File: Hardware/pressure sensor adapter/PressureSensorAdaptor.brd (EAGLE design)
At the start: 29.2 x 30.5 mm, 11 parts, among them IC1 RCV420P

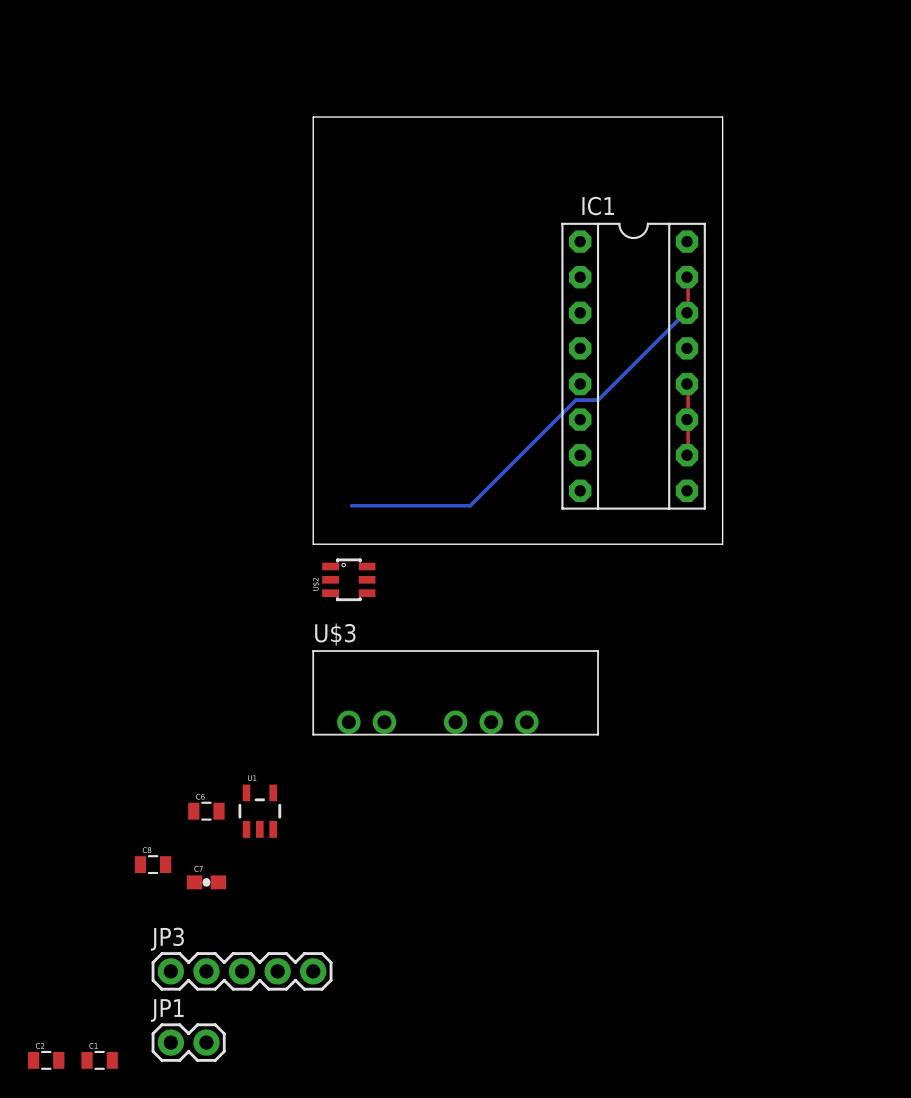
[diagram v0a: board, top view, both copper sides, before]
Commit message: routed alternet Pressure sense adapter board
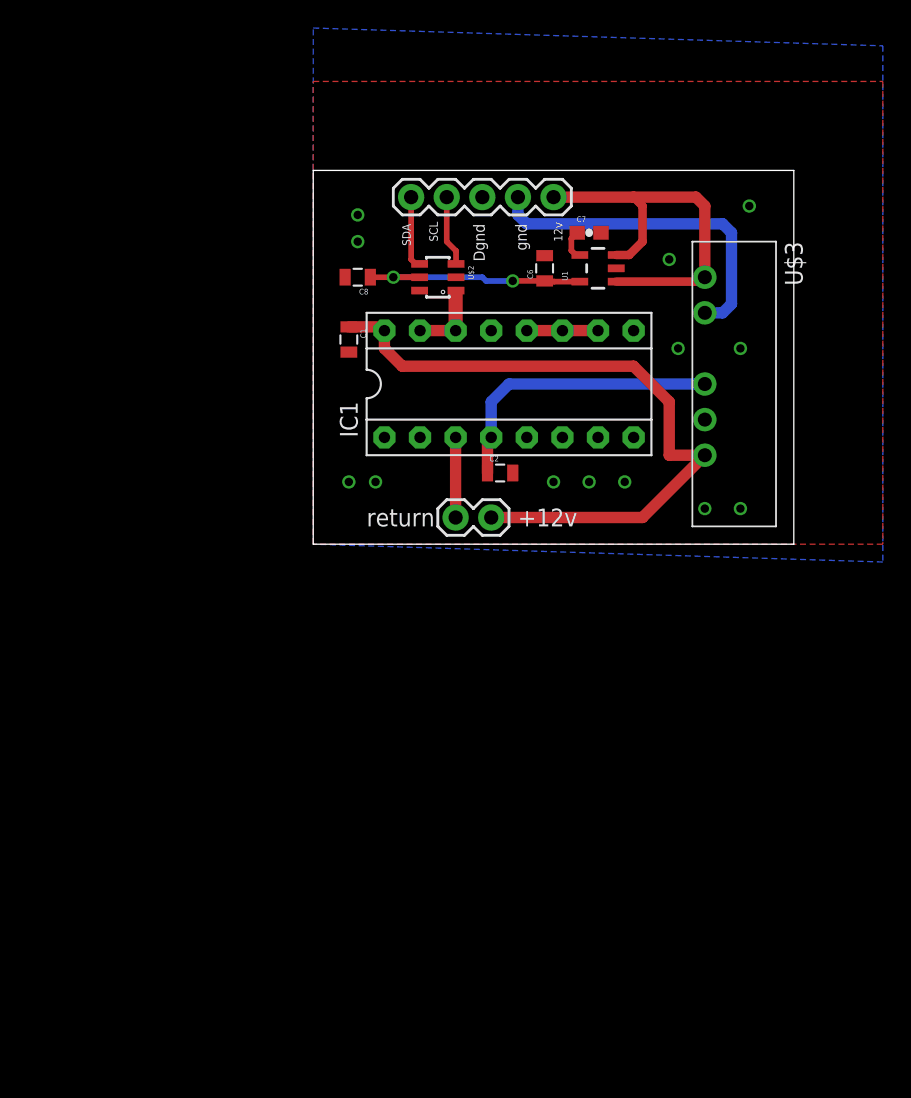
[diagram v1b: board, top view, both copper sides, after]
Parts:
- moved JP3 57.8 mm to (6.99, 24.8)
- moved C1 54.4 mm to (2.54, 14.6), turned to 270 degrees
- moved C7 53.8 mm to (19.7, 22.2)
- moved C2 53.0 mm to (13.3, 5.08)
- moved C6 45.6 mm to (16.5, 19.7), turned to 90 degrees
- moved U1 45.6 mm to (20.3, 19.7), turned to 90 degrees
- moved C8 44.4 mm to (3.17, 19.1), turned to 180 degrees
- moved JP1 42.6 mm to (10.2, 1.91)
- moved U$3 40.7 mm to (27.9, 19.1), turned to 270 degrees
- moved U$2 22.5 mm to (8.89, 19.1), turned to 180 degrees
- moved IC1 8.98 mm to (14.0, 11.4), turned to 0 degrees
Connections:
- removed net VIN: JP3.5, U$3.P$1, U1.1, U1.3
- new net 12V+: C1.1, IC1.16, JP1.2, U$3.P$6
- new net 12V-: C2.1, IC1.4, U$3.P$4
- net 12V: now also JP3.5, U$3.P$1, U1.1, U1.3; no longer C1.1, C2.1, IC1.16, IC1.4, JP1.2, U$3.P$4, U$3.P$6
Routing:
- net 12V+: track 0.00 -> 49.2 mm
- net 12V: track 0.00 -> 28.3 mm
- net GND: track 0.00 -> 24.3 mm
- net VOUT: track 32.2 -> 7.95 mm
- net 12V-: track 0.00 -> 21.0 mm
- net 5V: track 0.00 -> 16.9 mm, vias 0 -> 2
- net N$2: track 0.00 -> 5.71 mm
- net SDA: track 0.00 -> 5.18 mm
- net SCL: track 0.00 -> 5.04 mm
- net N$11: track 0.00 -> 2.18 mm
- added copper zone on layer 1, net GND-ISO
- added copper zone on layer 16, net GND-ISO
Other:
- board size 29.2 x 30.5 mm -> 34.3 x 26.7 mm
- board text added: "+12v"
- board text added: "12v"
- board text added: "Dgnd"
- board text added: "SCL"
- board text added: "SDA"
- board text added: "gnd"
- board text added: "return"

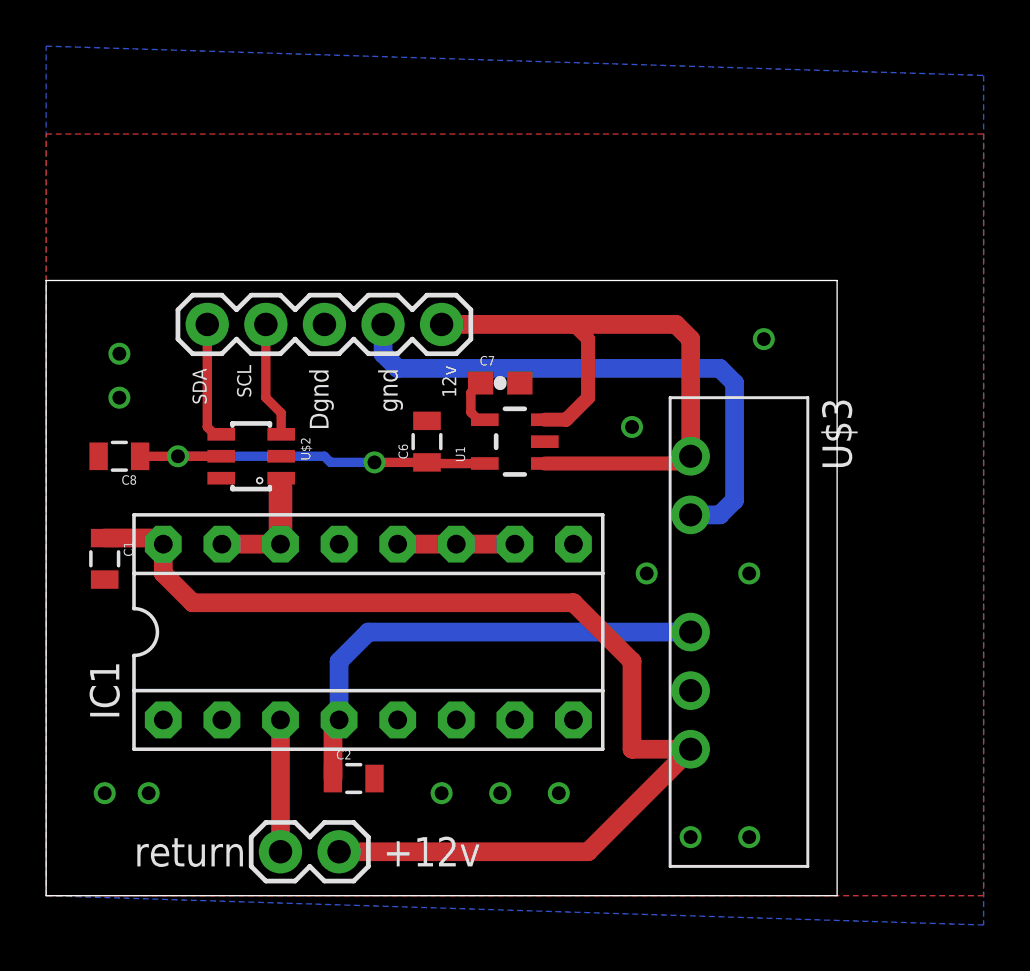
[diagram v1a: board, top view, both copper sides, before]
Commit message: added frame and logo to loayout
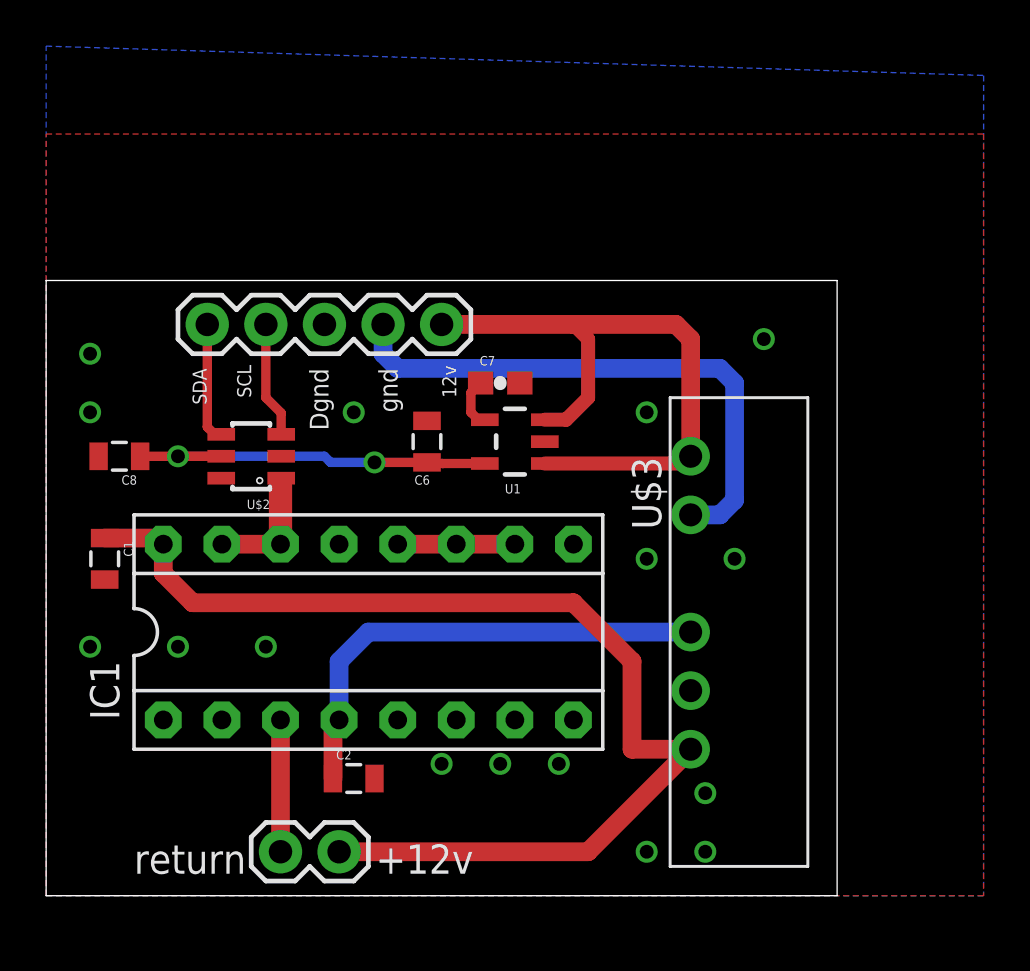
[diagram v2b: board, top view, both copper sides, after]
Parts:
- added FRAME1: FRAME-LEDGER, SparkFun-Aesthetics:CREATIVE_COMMONS
- added U$1: (no value), RitLaunchInitiative:RITLAUNCH_LOGO_SMALLB
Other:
- board text added: "Pressure sensor Adapter"
- board text added: "RIT Launch Initative"
- board text added: "Rev:A"
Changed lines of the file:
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@@
 <setting verticaltext="up"/>
 </settings>
-<grid distance="1.27" unitdist="mm" unit="mm" style="lines" multiple="1" display="yes" altdistance="0.025" altunitdist="inch" altunit="inch"/>
+<grid distance="1.27" unitdist="mm" unit="inch" style="lines" multiple="1" display="yes" altdistance="0.0125" altunitdist="inch" altunit="inch"/>
 <layers>
 <layer number="1" name="Top" color="4" fill="1" visible="yes" active="yes"/>
@@
 <wire x1="34.29" y1="26.67" x2="0" y2="26.67" width="0" layer="20"/>
 <wire x1="0" y1="26.67" x2="0" y2="0" width="0" layer="20"/>
-<text x="14.605" y="1.27" size="1.27" layer="21">+12v</text>
-<text x="3.81" y="1.27" size="1.27" layer="21">return</text>
+<text x="14.2875" y="0.9525" size="1.27" layer="21">+12v</text>
+<text x="3.81" y="0.9525" size="1.27" layer="21">return</text>
 <text x="6.35" y="22.86" size="0.6096" layer="21" rot="R270">SDA</text>
 <text x="8.89" y="21.59" size="0.6096" layer="21" rot="R90">SCL</text>
@@
 <text x="11.43" y="22.86" size="0.8128" layer="21" rot="R270">Dgnd</text>
 <text x="15.24" y="20.955" size="0.8128" layer="21" rot="R90">gnd</text>
+<text x="31.75" y="1.5875" size="1.27" layer="22" rot="MR90">Pressure sensor Adapter</text>
+<text x="30.1625" y="18.0975" size="0.8128" layer="22" rot="MR90">Rev:A</text>
+<text x="31.115" y="11.7475" size="0.8128" layer="22" rot="MR270">RIT Launch Initative</text>
 </plain>
 <attributes>
@@
 </class>
 </classes>
-<designrules name="LaenPCBOrder">
+<designrules name="LaenPCBOrder *">
 <description language="de">&lt;b&gt;EAGLE Design Rules&lt;/b&gt;
 &lt;p&gt;
@@
 <param name="mlMinCreamFrame" value="0mil"/>
 <param name="mlMaxCreamFrame" value="0mil"/>
-<param name="mlViaStopLimit" value="0mil"/>
+<param name="mlViaStopLimit" value="15mil"/>
 <param name="srRoundness" value="0"/>
 <param name="srMinRoundness" value="0mil"/>
@@
 </autorouter>
 <elements>
-<element name="IC1" library="burr-brown" package="DIL16" value="RCV420P" x="13.97" y="11.43">
+<element name="IC1" library="burr-brown" package="DIL16" value="RCV420P" x="13.97" y="11.43" smashed="yes">
 <attribute name="OC_NEWARK" value="60K6765" x="13.97" y="11.43" size="1.778" layer="27" display="off"/>
 <attribute name="MPN" value="RCV420JP" x="13.97" y="11.43" size="1.778" layer="27" display="off"/>
 <attribute name="MF" value="TEXAS INSTRUMENTS" x="13.97" y="11.43" size="1.778" layer="27" display="off"/>
 <attribute name="OC_FARNELL" value="1212342" x="13.97" y="11.43" size="1.778" layer="27" display="off"/>
-</element>
-<element name="U$2" library="RitLaunchInitiative" package="SOT23-6" value="MCP3425" x="8.89" y="19.05" rot="R180"/>
+<attribute name="VALUE" x="14.9225" y="9.2075" size="1.27" layer="27" ratio="10"/>
+<attribute name="NAME" x="3.175" y="7.62" size="1.27" layer="25" ratio="10" rot="R90"/>
+</element>
+<element name="U$2" library="RitLaunchInitiative" package="SOT23-6" value="MCP3425" x="8.89" y="19.05" smashed="yes" rot="R180">
+<attribute name="NAME" x="8.6995" y="16.764" size="0.4064" layer="25"/>
+</element>
 <element name="U$3" library="RitLaunchInitiative" package="VASD1-S12-D12-SIP" value="VASD1-S12-D12-SIP" x="27.94" y="19.05" smashed="yes" rot="R270">
-<attribute name="NAME" x="33.655" y="21.59" size="1.27" layer="25" rot="R270"/>
-<attribute name="VALUE" x="31.115" y="18.415" size="1.27" layer="27" rot="R270"/>
-</element>
-<element name="U1" library="SparkFun-PowerIC" package="SOT23-5" value="" x="20.32" y="19.685" rot="R90">
+<attribute name="NAME" x="26.67" y="15.875" size="1.27" layer="25" rot="R90"/>
+</element>
+<element name="U1" library="SparkFun-PowerIC" package="SOT23-5" value="" x="20.32" y="19.685" smashed="yes" rot="R90">
 <attribute name="PROD_ID" value="VREG-00823" x="20.32" y="19.685" size="1.778" layer="27" rot="R90" display="off"/>
-</element>
-<element name="C6" library="SparkFun-Capacitors" package="0805" value="2.2uF" x="16.51" y="19.685" rot="R90">
+<attribute name="NAME" x="20.574" y="17.8435" size="0.4064" layer="25" rot="R180"/>
+<attribute name="VALUE" x="20.5105" y="18.7325" size="0.4064" layer="27" rot="R90"/>
+</element>
+<element name="C6" library="SparkFun-Capacitors" package="0805" value="2.2uF" x="16.51" y="19.685" smashed="yes" rot="R90">
 <attribute name="PROD_ID" value="CAP-11624" x="16.51" y="19.685" size="1.778" layer="27" rot="R90" display="off"/>
-</element>
-<element name="C7" library="SparkFun-Capacitors" package="0603-CAP" value="470pF" x="19.685" y="22.225">
+<attribute name="NAME" x="16.637" y="18.2245" size="0.4064" layer="25" rot="R180"/>
+</element>
+<element name="C7" library="SparkFun-Capacitors" package="0603-CAP" value="470pF" x="19.685" y="22.225" smashed="yes">
 <attribute name="PROD_ID" value="CAP-07884" x="19.685" y="22.225" size="1.778" layer="27" display="off"/>
+<attribute name="NAME" x="18.796" y="22.987" size="0.4064" layer="25" font="vector"/>
 </element>
 <element name="C8" library="SparkFun-Capacitors" package="0805" value="" x="3.175" y="19.05" rot="R180"/>
@@
 <attribute name="PROD_ID" value="CAP-11625" x="13.335" y="5.08" size="1.778" layer="27" display="off"/>
 </element>
+<element name="FRAME1" library="SparkFun-Aesthetics" package="CREATIVE_COMMONS" value="FRAME-LEDGER" x="-5.08" y="-3.81">
+<attribute name="VERSION" value="A" x="-5.08" y="-3.81" size="1.778" layer="27" display="off"/>
+<attribute name="DESIGNER" value="Roy Cohen" x="-5.08" y="-3.81" size="1.778" layer="27" display="off"/>
+</element>
+<element name="U$1" library="RitLaunchInitiative" package="RITLAUNCH_LOGO_SMALLB" value="" x="20.32" y="13.97"/>
 </elements>
 <signals>
@@
 <vertex x="0" y="36.83"/>
 <vertex x="40.64" y="35.56"/>
-<vertex x="40.64" y="-1.27"/>
+<vertex x="40.64" y="0"/>
 <vertex x="0" y="0"/>
 </polygon>
-<via x="25.4" y="20.32" extent="1-16" drill="0.6" shape="octagon"/>
-<via x="22.225" y="4.445" extent="1-16" drill="0.6" shape="octagon"/>
-<via x="19.685" y="4.445" extent="1-16" drill="0.6" shape="octagon"/>
-<via x="17.145" y="4.445" extent="1-16" drill="0.6" shape="octagon"/>
-<via x="3.175" y="23.495" extent="1-16" drill="0.6" shape="octagon"/>
-<via x="3.175" y="21.59" extent="1-16" drill="0.6" shape="octagon"/>
-<via x="2.54" y="4.445" extent="1-16" drill="0.6" shape="octagon"/>
-<via x="4.445" y="4.445" extent="1-16" drill="0.6" shape="octagon"/>
-<via x="27.94" y="2.54" extent="1-16" drill="0.6" shape="octagon"/>
-<via x="30.48" y="2.54" extent="1-16" drill="0.6" shape="octagon"/>
-<via x="30.48" y="13.97" extent="1-16" drill="0.6" shape="octagon"/>
-<via x="26.035" y="13.97" extent="1-16" drill="0.6" shape="octagon"/>
+<via x="26.035" y="20.955" extent="1-16" drill="0.6" shape="octagon"/>
+<via x="22.225" y="5.715" extent="1-16" drill="0.6" shape="octagon"/>
+<via x="19.685" y="5.715" extent="1-16" drill="0.6" shape="octagon"/>
+<via x="17.145" y="5.715" extent="1-16" drill="0.6" shape="octagon"/>
+<via x="1.905" y="23.495" extent="1-16" drill="0.6" shape="octagon" alwaysstop="yes"/>
+<via x="1.905" y="20.955" extent="1-16" drill="0.6" shape="octagon" alwaysstop="yes"/>
+<via x="28.575" y="4.445" extent="1-16" drill="0.6" shape="octagon"/>
+<via x="28.575" y="1.905" extent="1-16" drill="0.6" shape="octagon"/>
+<via x="26.035" y="14.605" extent="1-16" drill="0.6" shape="octagon"/>
 <via x="31.115" y="24.13" extent="1-16" drill="0.6" shape="octagon"/>
+<via x="13.335" y="20.955" extent="1-16" drill="0.6" shape="octagon"/>
+<via x="1.905" y="10.795" extent="1-16" drill="0.6" shape="octagon"/>
+<via x="5.715" y="10.795" extent="1-16" drill="0.6" shape="octagon"/>
+<via x="9.525" y="10.795" extent="1-16" drill="0.6" shape="octagon"/>
+<via x="26.035" y="1.905" extent="1-16" drill="0.6" shape="octagon"/>
+<via x="29.845" y="14.605" extent="1-16" drill="0.6" shape="octagon"/>
 </signal>
 <signal name="5V">
